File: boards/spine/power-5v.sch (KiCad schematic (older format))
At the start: 14 parts

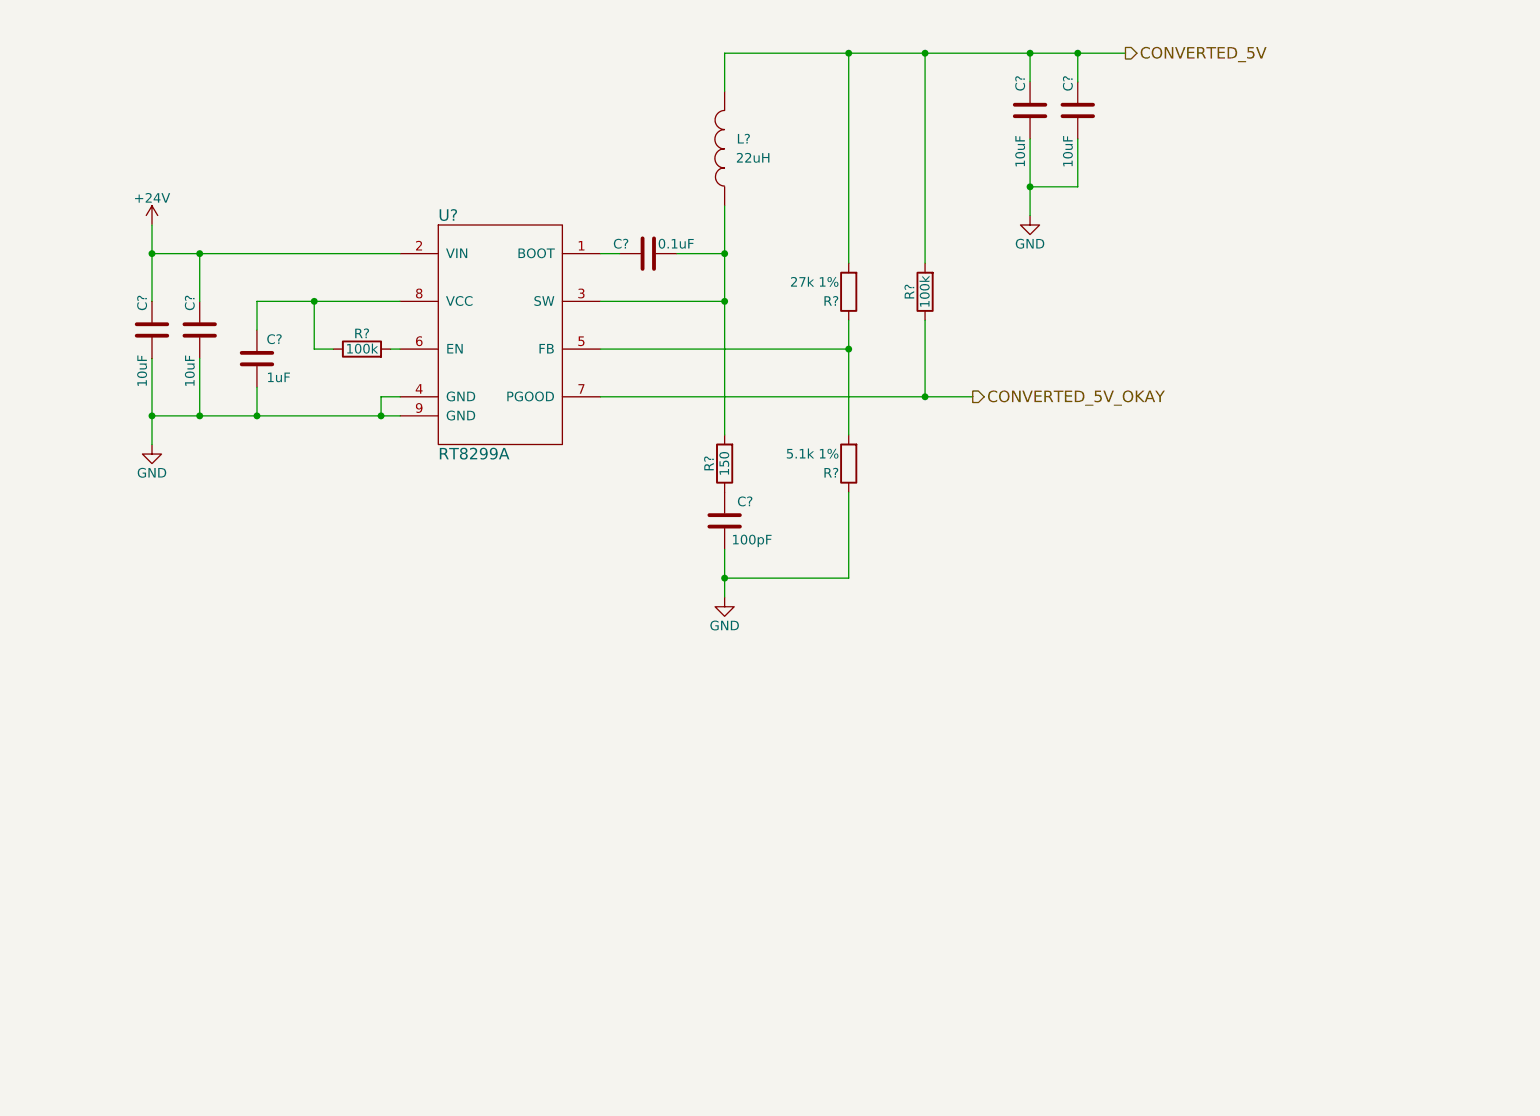
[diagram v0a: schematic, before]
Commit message: Power source switching
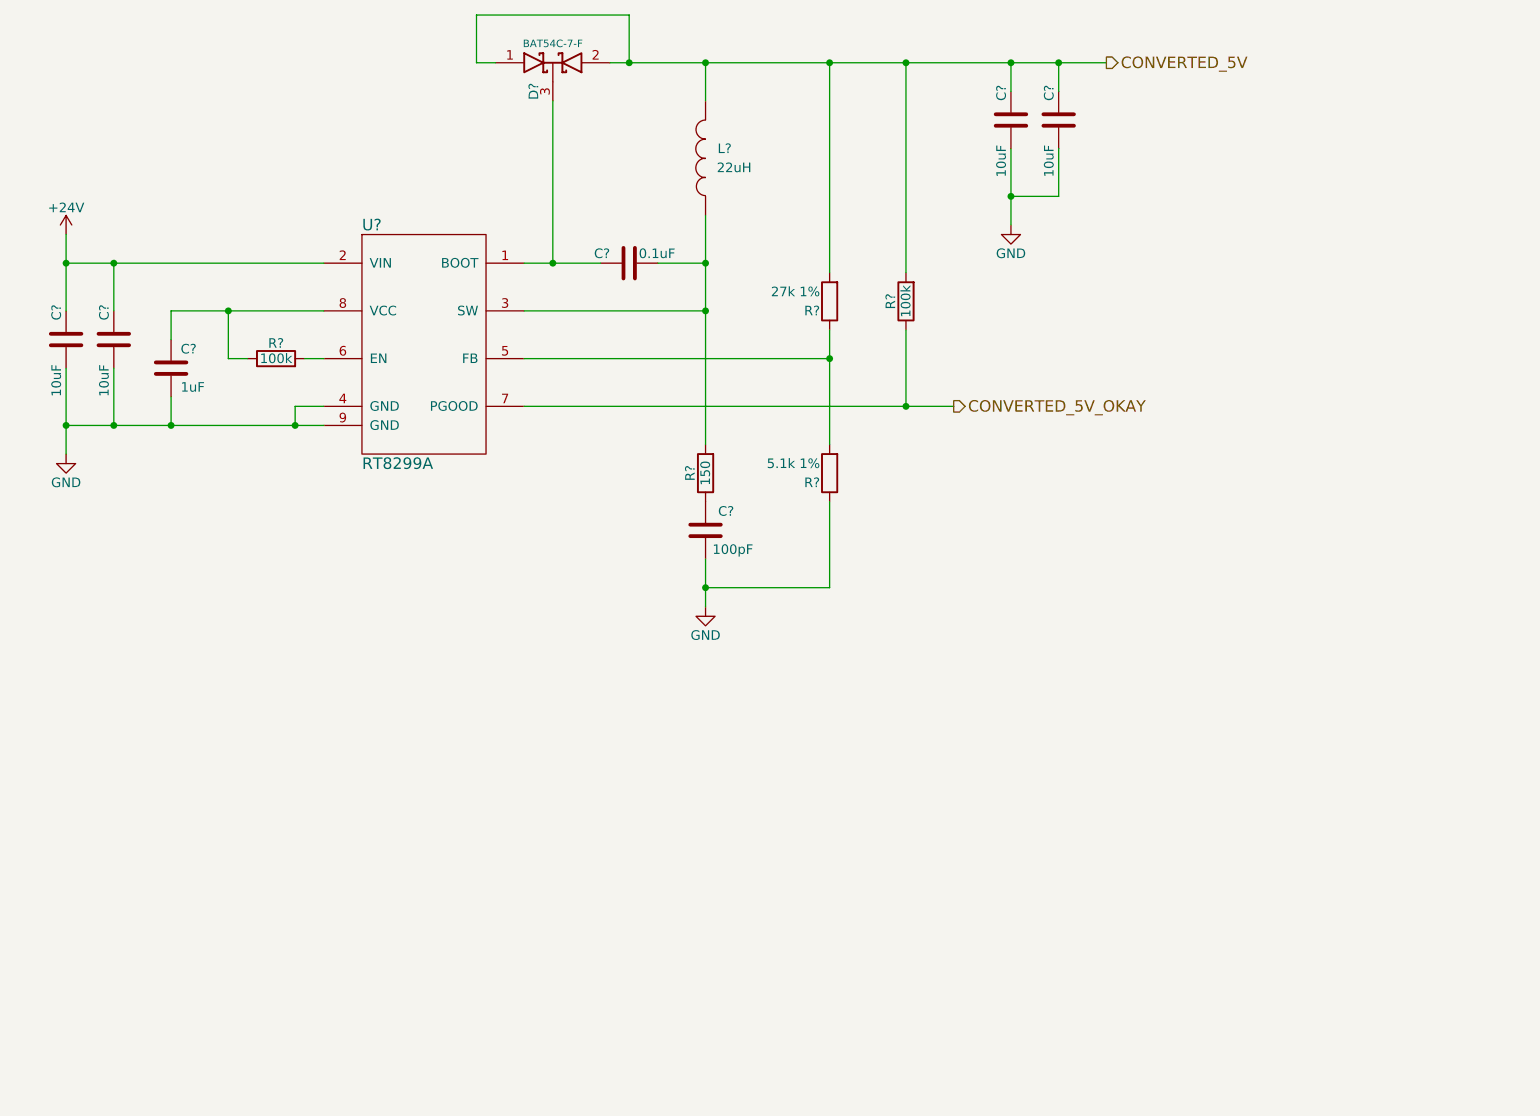
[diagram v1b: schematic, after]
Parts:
- added D?: BAT54 2x common cathode, symbol D_Schottky_x2_KCom_AAK
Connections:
- net CONVERTED_5V: now also D?.1 (A), D?.2 (A)
- net at C?.2, U?.1 (BOOT): now also D?.3 (K)
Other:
- moved on the sheet: C?, L?, R?, U?

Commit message: Power management and such
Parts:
- gave numbers to parts that had none: 15
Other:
- note added: "Bootstrap assistance for Vin < 5.5"
- note added: "Open drain output"
- moved on the sheet: C48, C49, C50, C51, C52, C53, C54, D5, L1, R20, R21, R22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

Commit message: Clock generator, sync connectors, title blocks
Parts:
- C48, C49, C53, C54: footprint 1206 -> Capacitors_SMD:C_1206
- C50, C51, C52: footprint 0805 -> Capacitors_SMD:C_0805
- R20, R21, R24: footprint (none) -> Resistors_SMD:R_0805
- R22, R23: footprint 0805 -> Resistors_SMD:R_0805
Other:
- note added: "A"
- note added: "High efficiency DC-DC converter,\n5V at 3A from 5-24V DC.\n\nThis 5V rail is shared by the USB output (up to 2A),\nthe modules (100mA each), and all FPGA and USB\ncontroller power rails."
- note added: "Wiggle Spine board"

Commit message: Schematic footprint and refdes work
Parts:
- D5: footprint (none) -> TO_SOT_Packages_SMD:SOT-23
- L1: footprint (none) -> Inductors_NEOSID:Neosid_Inductor_SM-NE127
- U8: footprint 8-SOP-EP -> Housings_SOIC:SOIC-8-1EP_3.9x4.9mm_Pitch1.27mm
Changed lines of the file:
@@
 $EndComp
 $Comp
-L GND #PWR0123
+L GND #PWR124
 U 1 1 564CA8D9
 P 2250 4800
-F 0 "#PWR0123" H 2250 4550 50  0001 C CNN
+F 0 "#PWR124" H 2250 4550 50  0001 C CNN
 F 1 "GND" H 2250 4650 50  0000 C CNN
 F 2 "" H 2250 4800 60  0000 C CNN
@@
 $EndComp
 $Comp
-L +24V #PWR0124
+L +24V #PWR123
 U 1 1 564CA8DB
 P 2250 3650
-F 0 "#PWR0124" H 2250 3500 50  0001 C CNN
+F 0 "#PWR123" H 2250 3500 50  0001 C CNN
 F 1 "+24V" H 2250 3790 50  0000 C CNN
 F 2 "" H 2250 3650 60  0000 C CNN
@@
 F 0 "U8" H 3800 3600 60  0000 L CNN
 F 1 "RT8299A" H 3800 2350 60  0000 L CNN
-F 2 "8-SOP-EP" H 4050 3600 60  0001 C CNN
+F 2 "Housings_SOIC:SOIC-8-1EP_3.9x4.9mm_Pitch1.27mm" H 4050 3600 60  0001 C CNN
 F 3 "http://www.richtek.com/assets/product_file/RT8299A/DS8299A-03.pdf" H 4050 3600 60  0001 C CNN
 F 4 "Digikey" H 4050 3600 60  0001 C CNN "Vend1"
@@
 F 0 "L1" H 5500 3200 50  0000 C CNN
 F 1 "22uH" H 5450 3300 50  0000 C CNN
-F 2 "" H 5600 3250 60  0001 C CNN
+F 2 "Inductors_NEOSID:Neosid_Inductor_SM-NE127" H 5600 3250 60  0001 C CNN
 F 3 "http://www.bourns.com/docs/Product-Datasheets/SRR1280.pdf" H 5600 3250 60  0001 C CNN
 F 4 "SRR1280-220MTR-ND" V 5600 3250 60  0001 C CNN "Vend1Id"
@@
 $EndComp
 $Comp
-L GND #PWR0125
+L GND #PWR126
 U 1 1 564CA8FA
 P 7200 3600
-F 0 "#PWR0125" H 7200 3350 50  0001 C CNN
+F 0 "#PWR126" H 7200 3350 50  0001 C CNN
 F 1 "GND" H 7200 3450 50  0000 C CNN
 F 2 "" H 7200 3600 60  0000 C CNN
@@
 $EndComp
 $Comp
-L GND #PWR0126
+L GND #PWR125
 U 1 1 564CC489
 P 5600 5600
-F 0 "#PWR0126" H 5600 5350 50  0001 C CNN
+F 0 "#PWR125" H 5600 5350 50  0001 C CNN
 F 1 "GND" H 5600 5450 50  0000 C CNN
 F 2 "" H 5600 5600 60  0000 C CNN
@@
 F 0 "D5" V 4700 2600 50  0000 C CNN
 F 1 "BAT54 2x common cathode" H 4800 2850 50  0001 C CNN
-F 2 "" H 4800 2750 60  0001 C CNN
+F 2 "TO_SOT_Packages_SMD:SOT-23" H 4800 2750 60  0001 C CNN
 F 3 "http://www.diodes.com/_files/datasheets/ds11005.pdf" H 4800 2750 60  0001 C CNN
 F 4 "Diodes Inc" H 4800 2900 39  0001 C CNN "MfrId"
@@
 FB 59 00 E6 A5 69 3A 37 9E CF 73 BC F7 37 E3 33 5D 9E A8 3E 7F 80 FA F7 F6 BB 44 F4 6E D4 E7 77
 A2 1E 1F 27 A2 E3 16 70 32 E9 54 FE 3F E7 AF 00 CA 1C A3 36 0A 00 00 00 00 49 45 4E 44 AE 42 60
-82 70
+82 00
 EndData
 $EndBitmap
